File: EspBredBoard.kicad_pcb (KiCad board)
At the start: 2 copper layers, 31.6 x 46 mm, 29 parts, among them J1 USB_C_Receptacle_USB2.0, J2 USB_C_Receptacle_USB2.0, J3 Conn_01x17, J4 Conn_01x17, SW1 TS-1145A-B-A, SW2 TS-1145A-B-A, U1 CH343P, U2 ESP32-S2-WROOM-I(4M), U3 ME6217C33M5G

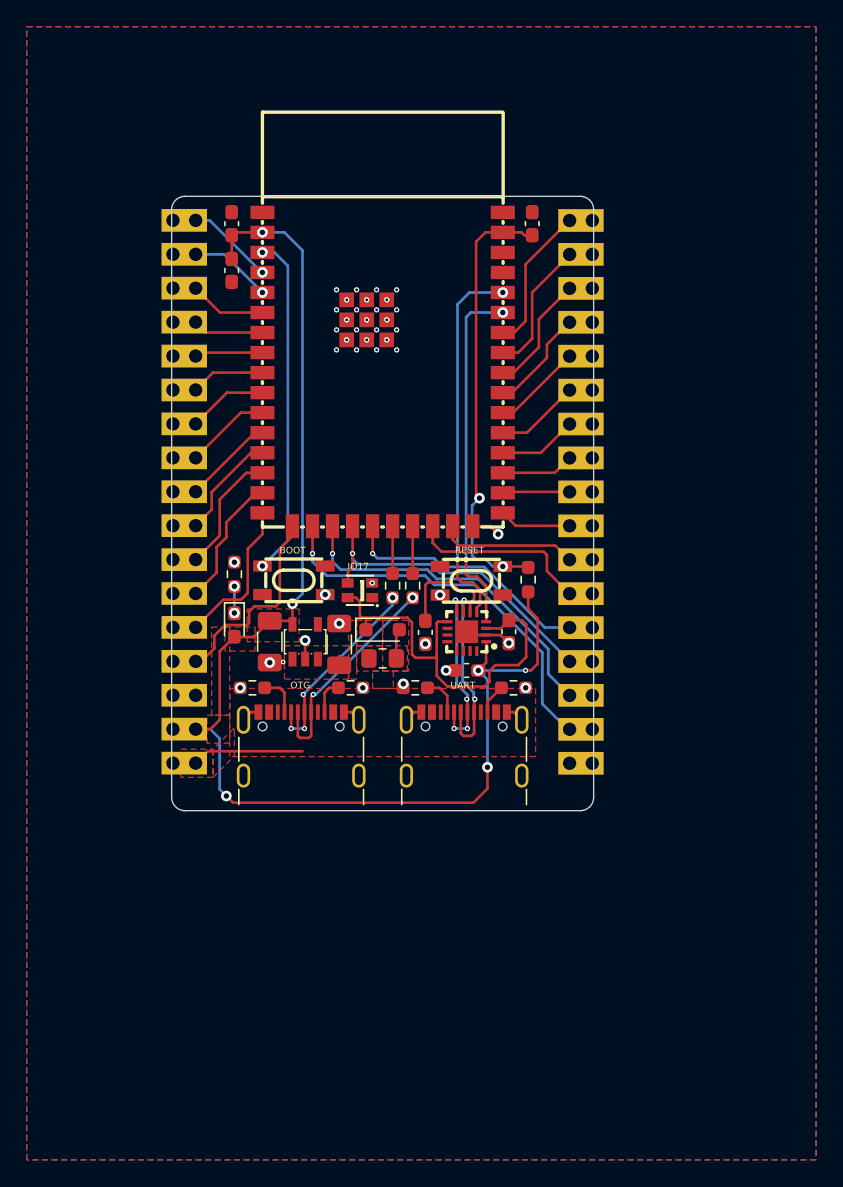
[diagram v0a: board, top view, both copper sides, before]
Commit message: fix wrong uart route - add uart test point - add vin led
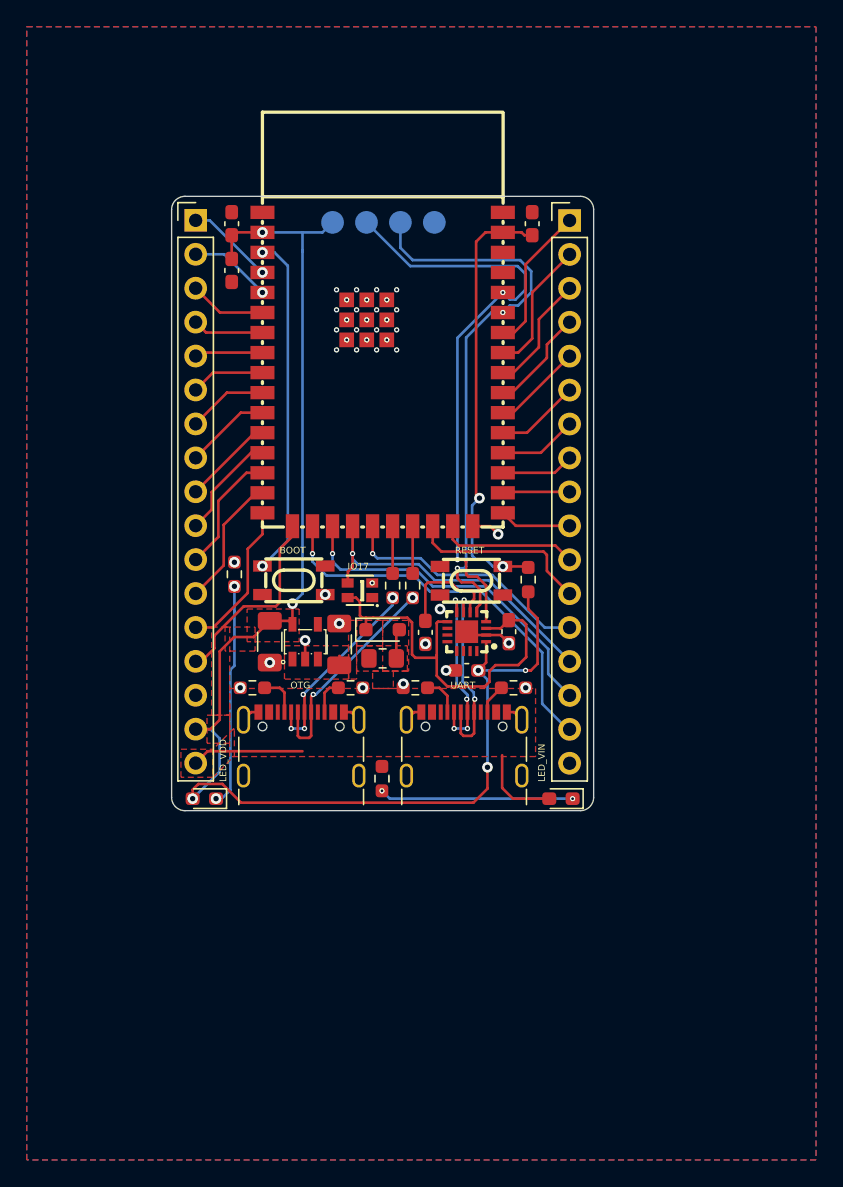
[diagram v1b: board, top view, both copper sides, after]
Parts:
- added D3: LED, LED_SMD:LED_0603_1608Metric_Pad1.05x0.95mm_HandSolder, F.Cu at (150.2, 112.6)
- added J5: UART_TEST_POINT, Connector_PinHeader_2.54mm:PinHeader_1x04_P2.54mm_Vertical, B.Cu at (133.2, 69.5)
- added R9: 300, Resistor_SMD:R_0603_1608Metric_Pad0.98x0.95mm_HandSolder, F.Cu at (136.8, 111.1)
- C1, C2, C3, C6, C7, C8: footprint Library:C_0603_1608Metric_Pad1.08x0.95mm_HandSolder -> Capacitor_SMD:C_0603_1608Metric_Pad1.08x0.95mm_HandSolder
- C4, C5: footprint Library:C_1206_3216Metric_Pad1.33x1.80mm_HandSolder -> Capacitor_SMD:C_1206_3216Metric_Pad1.33x1.80mm_HandSolder
- D1: footprint Library:D_SOD-323_HandSoldering -> Diode_SMD:D_SOD-323_HandSoldering
- D2: footprint Library:LED_0603_1608Metric_Pad1.05x0.95mm_HandSolder -> LED_SMD:LED_0603_1608Metric_Pad1.05x0.95mm_HandSolder
- F1: footprint Library:Fuse_0805_2012Metric_Pad1.15x1.40mm_HandSolder -> Fuse:Fuse_0805_2012Metric_Pad1.15x1.40mm_HandSolder
- J1, J2: footprint Library:USB_C_Receptacle_GCT_USB4105-xx-A_16P_TopMnt_Horizontal -> Connector_USB:USB_C_Receptacle_GCT_USB4105-xx-A_16P_TopMnt_Horizontal
- J3, J4: footprint Library:PinHeader_1x17_P2.54mm_Vertical -> Connector_PinHeader_2.54mm:PinHeader_1x17_P2.54mm_Vertical
- R1, R2, R3, R4, R5, R6, R7, R8: footprint Library:R_0603_1608Metric_Pad0.98x0.95mm_HandSolder -> Resistor_SMD:R_0603_1608Metric_Pad0.98x0.95mm_HandSolder
- moved D2 13.2 mm to (123.5, 112.6), turned to 180 degrees
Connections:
- U1 pad 4: /UART_TXD -> /UART_RXD
- U1 pad 5: /UART_RXD -> /UART_TXD
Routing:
- net /UART_RXD: track 28.1 -> 44.5 mm
- net /UART_TXD: track 26.7 -> 42.7 mm
- net Net-(D2-K): track 2.00 -> 16.9 mm
- net Net-(D3-K): track 0.00 -> 14.5 mm, vias 0 -> 2
- net VDD: track 98.4 -> 106.4 mm
- net /VIN: track 8.37 -> 14.7 mm
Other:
- board text added: "3V3"
- board text added: "LED_VDD"
- board text added: "LED_VIN"
- board text added: "RXD"
- board text added: "TXD"
